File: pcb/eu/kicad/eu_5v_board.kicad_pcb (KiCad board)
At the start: 2 copper layers, 57.9 x 27.9 mm, 6 parts, among them J1 Socket 1x2 2.54, P1 P70-2200045 GND, P2 P70-2200045 +5V

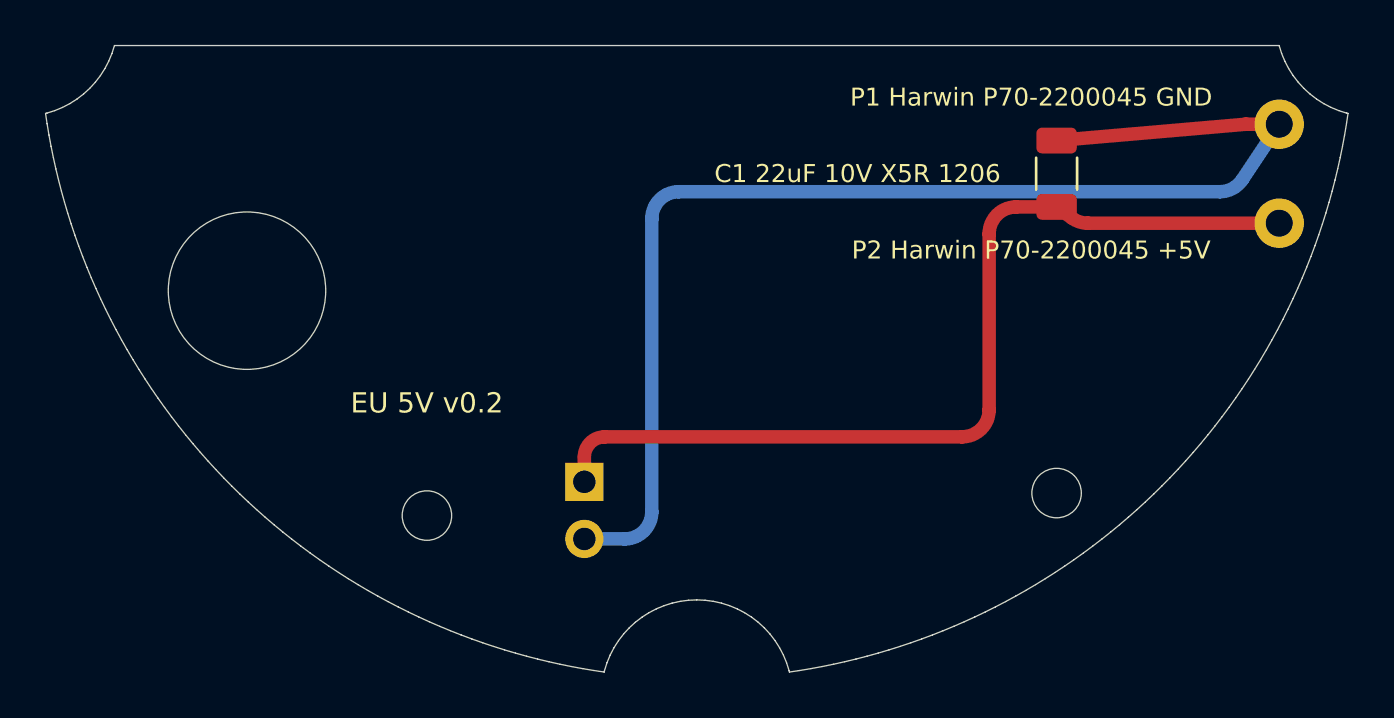
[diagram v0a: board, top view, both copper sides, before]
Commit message: Boards for v0.4: ring board, mic carrier, riser, cover flex, EU cap board, wiring board posts
- Ring board, mic carrier and riser in pcb/sensor/ (D-50, D-60, D-68); carrier and riser fab
  packs; the ring board waits on the MSR-2's CN2 part and map
- Riser 14 x 12 mm, pins above and between the posts; cover flex with the run past the GND
  contact post and a jog from the pad section (D-79)
- EU cap board on the carrier, closed snap windows, wider with the face plate (D-56, D-70,
  D-77, D-78); EU 5 V board pins follow the back cover's pads
- Wiring board: WA-SMSI spacer posts in the 5 V area (SMT, spigot inside the board), J2
- ERC / DRC clean on every board
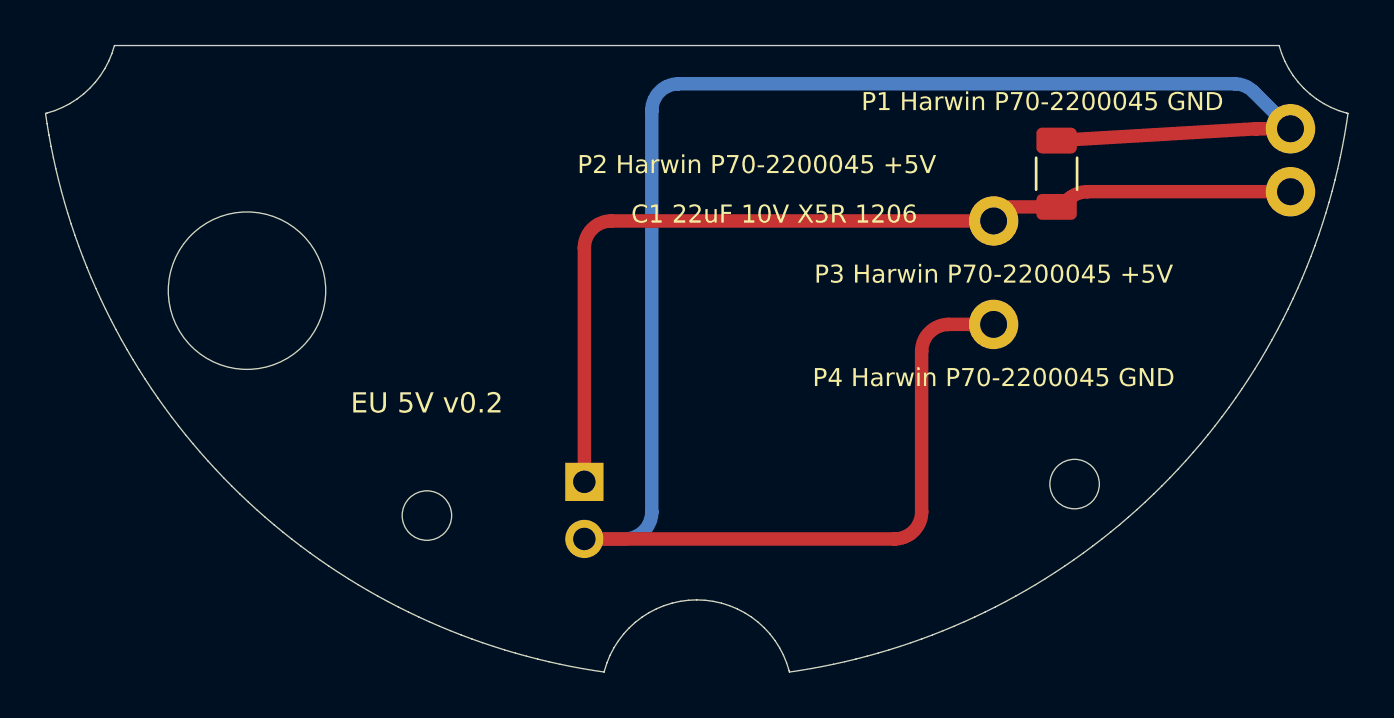
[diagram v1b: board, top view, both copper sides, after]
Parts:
- added P3: P70-2200045 +5V, eu:Harwin_P70-2200045, F.Cu at (113.2, 108.9)
- added P4: P70-2200045 GND, eu:Harwin_P70-2200045, F.Cu at (113.2, 113.5)
- moved P2 1.49 mm to (126.4, 107.6)
- moved MH2 0.89 mm to (116.8, 120.6)
- moved P1 0.54 mm to (126.4, 104.8)
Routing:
- net GND: track 56.6 -> 88.3 mm
- net +5V: track 41.8 -> 43.0 mm
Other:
- board text added: "P3 Harwin P70-2200045 +5V"
- board text added: "P4 Harwin P70-2200045 GND"

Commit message: Board generators: shared P70 and WA-SMSI footprints, fixed revision date, EU boards v0.4
- One Harwin P70 footprint with its 3D model for the riser and the EU 5 V board; one
  WA-SMSI land pattern for the wiring board posts and the ring board spacers
- Shared library-table and symbol helpers; dead code from removed boards gone
- REV_DATE replaces today's date on silkscreen and title blocks
- EU boards v0.4; EU cap board fab pack written once CN2 is confirmed
- Order lists key the EU header as TSM-102-02-L-SV (D-59)
- ERC / DRC clean on every board
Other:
- board text added: "EU 5V v0.4"
- board text removed: "EU 5V v0.2"

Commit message: Mic on the boards, parts audit, rocker second source, CN2 land pattern, back cover fit (D-82..D-90)
- Prototype PCBWay packs for the ring board, EU cap board and cover flex; logos and URL on the
  boards with room for them
- CN2 mate: Molex 55909-2474 on an assumed 51338-2474 (D-82); land pattern from Molex
  SD-55909-003 rev J, B2B from SD-51338-003 rev K (D-89); contact map and pin 1 still open
- Microphone: Knowles SPK0641HT4H-1 + ADAU7002 on the ring board and the EU cap board, the mic
  carrier removed; face plate sound column on a gasket (D-83); C3 KEMET C1206C104J3GACTU C0G
  (D-85)
- Parts rule (active, stocked at DigiKey or Mouser) and audit: F1 3403.0166.11, cover flex 1 uF
  CL05A105KO5NNNC, rocker at Mouser 979-1802.2504 (D-84)
- Rocker: tabs soldered into plated slots accepted (D-86); E-Switch RA412C1100 second source,
  slotted footprint on the wiring board and the EU mains board, solder the rocker after the
  board is screwed down (D-88)
- Back cover: round-over 8.1 x 8.0 from the printed gauges (D-87); four tabs inside the long
  side walls into the housing's slots (D-90); back_gauges_PLA
- make stock / make order-push (pcb/tools/distributors.py): live DigiKey / Mouser stock and
  lifecycle, DigiKey myLists link and Mouser cart; keys from the environment only
- Boards ERC / DRC clean; make check, make eu, make check-renders pass; renders, fab and
  order packs regenerated
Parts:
- added LOGO1: Ant_Logo_8mm_SilkScreen, eu:Ant_Logo_8mm_SilkScreen, B.Cu at (90.1, 106.7)
- added LOGO2: KiCad-Logo2_5mm_SilkScreen, eu:KiCad-Logo2_5mm_SilkScreen, B.Cu at (102.4, 105.7)
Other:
- board text added: "github.com/antevens/smart-wallplate"

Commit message: Parts and order lists: EU PE connector, 22 uF C1, unit and devkit lists, E-Switch rocker (D-94, D-95, D-97)
- D-94: the EU lights' PE joined in the box in a WAGO 221-412 (EXTRA_EU, ASSEMBLY step 5); the
  boards carry no PE; the steel piece's insulation added to the EU review checklist
- D-95: 22 uF C1 KEMET C1206C226M4PACTU (16 V X5R, 1.8 max) on the ring board, the EU cap board
  and the EU 5 V board; the Samsung CL31A226KPHNNNE has a 61-week maker lead time
- D-97: make order writes unit_na, unit_eu, devkit_na, devkit_eu (4 sets per variant,
  DEVKIT_SETS), exact counts; the PCBWay packs are the devkit (5 PCBs per design); the old
  3 NA + 2 EU lists removed
- Rocker: both variants' lists take the E-Switch RA412C1100 (RA4 datasheet rating option C:
  UL/cUL 10 A 250 VAC; ENEC 10(4) A 250 V~); the Marquardt stays the reference part
- ADAU7002 to DigiKey in Mouser orders (Mouser does not restock it); stale PCBWay notes fixed
- Boards ERC / DRC clean; renders regenerated
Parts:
- C1: value 22uF 10V X5R -> 22uF 16V X5R
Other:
- board text added: "C1 22uF 16V X5R 1206"
- board text removed: "C1 22uF 10V X5R 1206"

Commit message: EU PSU: Zettler ZPI03S0500WC instead of the Traco TMPS 03-105 (D-100)
- 8.72 against 24.09 CAD at DigiKey (an EU plate's parts 63.54, was 78.91); 5 V 600 mA,
  I/P-O/P 3600 VAC, UL/EN 62368-1; body 25 x 25 x 16 +-0.5 (PSU the maximum)
- Footprint from Zettler's PCB layout (AC pins 15 apart, outputs 5 apart, rows 15 apart, 1.2
  holes), 4-pin symbol; the NC pin and its DRC rule removed
- Mains board re-laid: fused line track 3.5 from the N pin, relief slot y -15, 5 V header x 8.5
  beside V+, F1 (15.0, -2.5), front logos above the slot; both EU boards ERC / DRC clean,
  make eu passes
- Open for review: reinforced insulation and overvoltage category not stated; Zettler's input
  fuse 0.5 A (F1 is T1A); DigiKey stock 142
- Order lists, PCBWay packs and renders regenerated
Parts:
- moved J1 13.5 mm to (108.5, 120.5)
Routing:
- net GND: track 88.3 -> 61.6 mm
- net +5V: track 43.0 -> 29.5 mm

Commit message: v0.5: back cover ends, mains spacing 3.0 mm, NA fuse separation, labels, bare renders (D-101..D-106)
- D-101: back cover shell gauges (R15..R20.9); the stadium end is confirmed
- D-102: mains spacing 3.0 mm on high-CTI FR4 (MAINS_GAP, NA and EU)
- D-103: back cover end walls 1.40 mm, inside 0.2 mm longer (BC_END_WALL)
- D-104: NA wiring board: any two mains nets 3.0 mm apart, L_F re-routed
  F1.2 -> RV1.1, L_SW vias below F1, L_SW pour up towards the rocker;
  EU mains board checked, unchanged
- D-105: rocker silkscreen "E-Switch RA412C1100 or Marquardt 1802.2504",
  EU 5 V socket part on its label; bare 3D renders for every board
- D-106: version v0.5; v0.4 fab packs, PCBWay packs and renders removed
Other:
- board text added: "EU 5V v0.5"
- board text added: "J1 Samtec SSW-102-01-G-S"
- board text removed: "EU 5V v0.4"
- board text removed: "J1 +5V GND socket"
